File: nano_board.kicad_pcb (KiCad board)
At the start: 2 copper layers, 27 parts, among them J1 RJ45

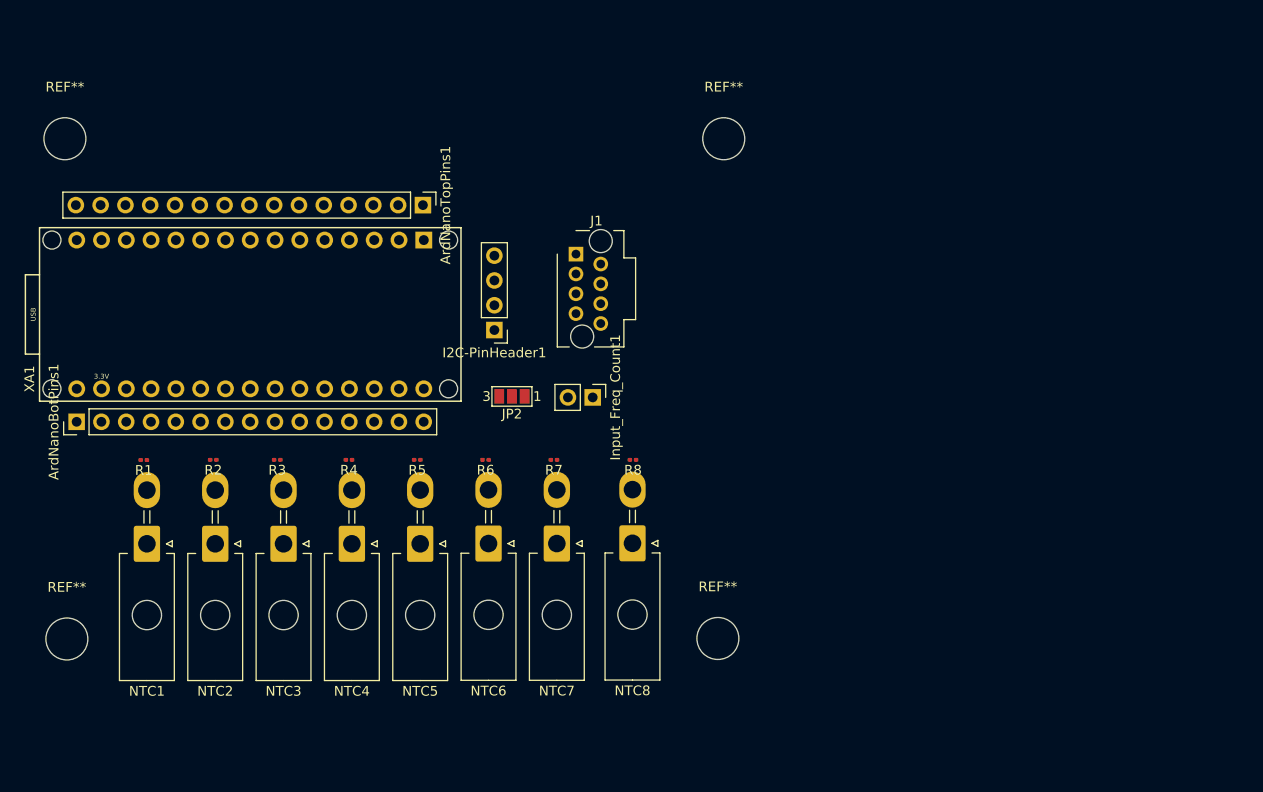
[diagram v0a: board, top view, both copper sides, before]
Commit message: ADD: schematic as pdf
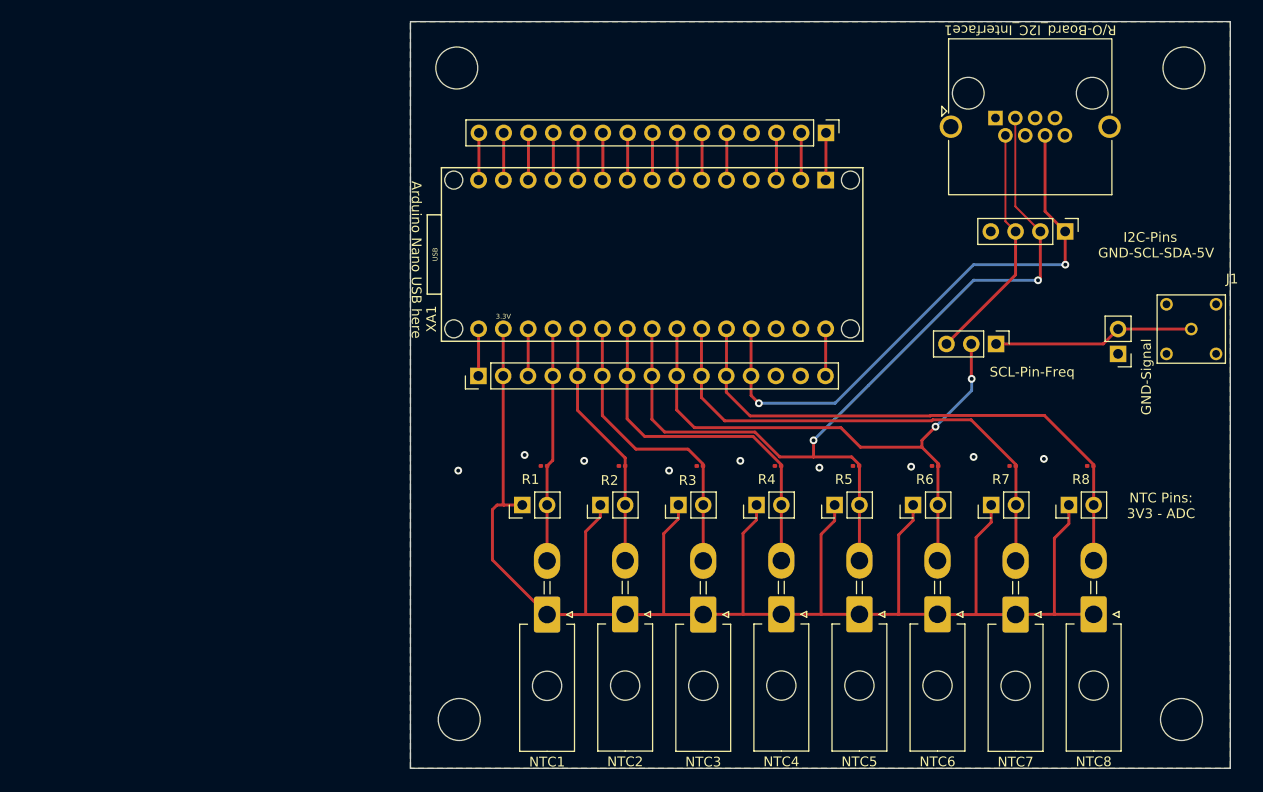
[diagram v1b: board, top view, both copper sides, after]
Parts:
- removed ArdNanoBotPins1: 01x15_Male, Connector_PinHeader_2.54mm:PinHeader_1x15_P2.54mm_Vertical
- removed ArdNanoTopPins1: Conn_01x15_Male, Connector_PinHeader_2.54mm:PinHeader_1x15_P2.54mm_Vertical
- removed I2C-PinHeader1: Conn_01x04_Male, Connector_PinHeader_2.54mm:PinHeader_1x04_P2.54mm_Vertical
- removed Input_Freq_Count1: Conn_01x02, Connector_PinHeader_2.54mm:PinHeader_1x02_P2.54mm_Vertical
- removed JP2: Jumper_A5, Jumper:SolderJumper-3_P1.3mm_Open_Pad1.0x1.5mm_NumberLabels
- removed the REF** at (121.5, 104.2)
- removed the REF** at (54.8, 104.2)
- removed the REF** at (54.6, 53.0)
- removed the REF** at (122.1, 53.0)
- added BottomsidePins Arduino: 01x15_Male, Connector_PinHeader_2.54mm:PinHeader_1x15_P2.54mm_Vertical, F.Cu at (97.0, 77.3)
- added GND-Signal: Conn_01x02, Connector_PinHeader_2.54mm:PinHeader_1x02_P2.54mm_Vertical, F.Cu at (162.5, 75.0)
- added I2C-Pins: Conn_01x04_Male, Connector_PinHeader_2.54mm:PinHeader_1x04_P2.54mm_Vertical, F.Cu at (157.1, 62.5)
- added NTC0-Pin1: Pin-Header 01x02, Connector_PinHeader_2.54mm:PinHeader_1x02_P2.54mm_Vertical, F.Cu at (101.5, 90.5)
- added NTC1-Pin1: Pin-Header 01x02, Connector_PinHeader_2.54mm:PinHeader_1x02_P2.54mm_Vertical, F.Cu at (109.5, 90.5)
- added NTC2-Pin1: Pin-Header 01x02, Connector_PinHeader_2.54mm:PinHeader_1x02_P2.54mm_Vertical, F.Cu at (117.5, 90.5)
- added NTC3-Pin1: Pin-Header 01x02, Connector_PinHeader_2.54mm:PinHeader_1x02_P2.54mm_Vertical, F.Cu at (125.5, 90.5)
- added NTC4-Pin1: Pin-Header 01x02, Connector_PinHeader_2.54mm:PinHeader_1x02_P2.54mm_Vertical, F.Cu at (133.5, 90.5)
- added NTC5-Pin1: Pin-Header 01x02, Connector_PinHeader_2.54mm:PinHeader_1x02_P2.54mm_Vertical, F.Cu at (141.5, 90.5)
- added NTC6-Pin1: Pin-Header 01x02, Connector_PinHeader_2.54mm:PinHeader_1x02_P2.54mm_Vertical, F.Cu at (149.5, 90.5)
- added NTC7-Pin1: Pin-Header 01x02, Connector_PinHeader_2.54mm:PinHeader_1x02_P2.54mm_Vertical, F.Cu at (157.5, 90.5)
- added R/O-Board_I2C_Interface1: RJ45, Connector_RJ:RJ45_Amphenol_RJHSE5380, F.Cu at (149.9, 50.9)
- added REF**: MountingHole_4.3mm_M4, MountingHole:MountingHole_4.3mm_M4, F.Cu at (95.0, 112.5)
- added REF**: MountingHole_4.3mm_M4, MountingHole:MountingHole_4.3mm_M4, F.Cu at (94.8, 45.8)
- added REF**: MountingHole_4.3mm_M4, MountingHole:MountingHole_4.3mm_M4, F.Cu at (169.2, 45.8)
- added REF**: MountingHole_4.3mm_M4, MountingHole:MountingHole_4.3mm_M4, F.Cu at (169.0, 112.5)
- added SCL-Pin-Freq: Conn_01x03_Male, Connector_PinHeader_2.54mm:PinHeader_1x03_P2.54mm_Vertical, F.Cu at (150.0, 74.0)
- added Topside Pins Arduino: Conn_01x15_Male, Connector_PinHeader_2.54mm:PinHeader_1x15_P2.54mm_Vertical, F.Cu at (132.6, 52.4)
- J1: value RJ45 -> LEMO2; footprint Connector_RJ:RJ45_Plug_Metz_AJP92A8813 -> OwnFootprints:EPL.00.250.NTN
- NTC1, NTC2, NTC3, NTC4, NTC5, NTC6, NTC7, NTC8: value Conn_01x02 -> Molex01x02
- moved J1 63.5 mm to (170.0, 72.5)
- moved NTC8 47.8 mm to (160.0, 101.7)
- moved NTC7 47.6 mm to (152.0, 101.8)
- moved R7 47.0 mm to (151.7, 86.5)
- moved R8 46.9 mm to (159.7, 86.5)
- moved NTC6 46.6 mm to (144.0, 101.7)
- moved R6 46.1 mm to (143.8, 86.5)
- moved NTC5 45.6 mm to (136.0, 101.7)
- moved R5 45.0 mm to (135.7, 86.5)
- moved NTC4 44.6 mm to (128.0, 101.7)
- moved R4 44.0 mm to (127.7, 86.5)
- moved NTC3 43.6 mm to (120.0, 101.8)
- moved R3 43.3 mm to (119.7, 86.5)
- moved NTC2 42.6 mm to (112.0, 101.7)
- moved R2 41.9 mm to (111.7, 86.5)
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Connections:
- J1 pad 1: GND -> Freq
- NTC5 pad 2: SDA -> A4
- NTC6 pad 2: A5_Pin -> A5
- R5 pad 1: SDA -> A4
- R6 pad 1: A5_Pin -> A5
- XA1 pad A4: SDA -> A4
- XA1 pad A5: A5_Pin -> A5
- XA1 pad RST2: RST2 -> unconnected-(XA1-PadRST2)
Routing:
- net 3V3_Ard: track 0.00 -> 173.2 mm
- net A4: track 0.00 -> 91.6 mm, vias 0 -> 2
- net A5: track 0.00 -> 60.1 mm, vias 0 -> 2
- net 5V_Ard: track 0.00 -> 59.4 mm, vias 0 -> 2
- net A7: track 0.00 -> 57.1 mm
- net A6: track 0.00 -> 52.1 mm
- net A3: track 0.00 -> 36.8 mm
- net A2: track 0.00 -> 31.2 mm
- net A1: track 0.00 -> 25.8 mm
- net SCL: track 0.00 -> 24.7 mm
- net A0: track 0.00 -> 24.0 mm
- net Freq: track 0.00 -> 20.6 mm
- net RST1: track 0.00 -> 4.85 mm
- net D9: track 0.00 -> 4.85 mm
- net D8: track 0.00 -> 4.85 mm
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- added copper zone on B.Cu, net GND
- added copper zone on F.Cu, net GND
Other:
- board outline added: 84 x 76.5 mm
- board text added: "Arduino Nano USB here"
- board text added: "GND-SCL-SDA-5V"
- board text added: "NTC Pins: 3V3 - ADC"
